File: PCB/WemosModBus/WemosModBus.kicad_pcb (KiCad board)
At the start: 2 copper layers, 38.1 x 60.3 mm, 12 parts, among them J1 Relay output, J2 Power, J3 Enable ModBus, M1 hw-726, U1 WeMos_mini, U2 MH-MINI-360

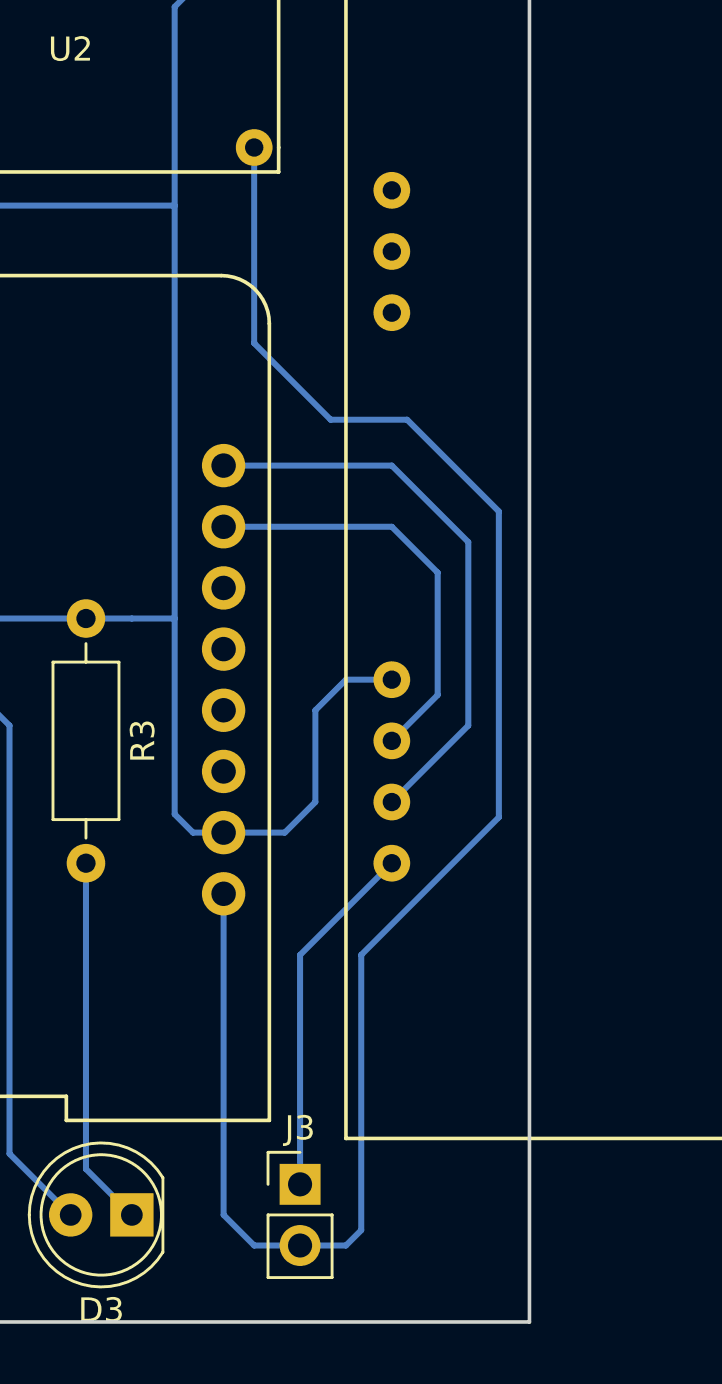
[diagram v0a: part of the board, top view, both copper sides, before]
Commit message: Made ModBus enable jumper break/connect TX instead of power to the TTL circuit.
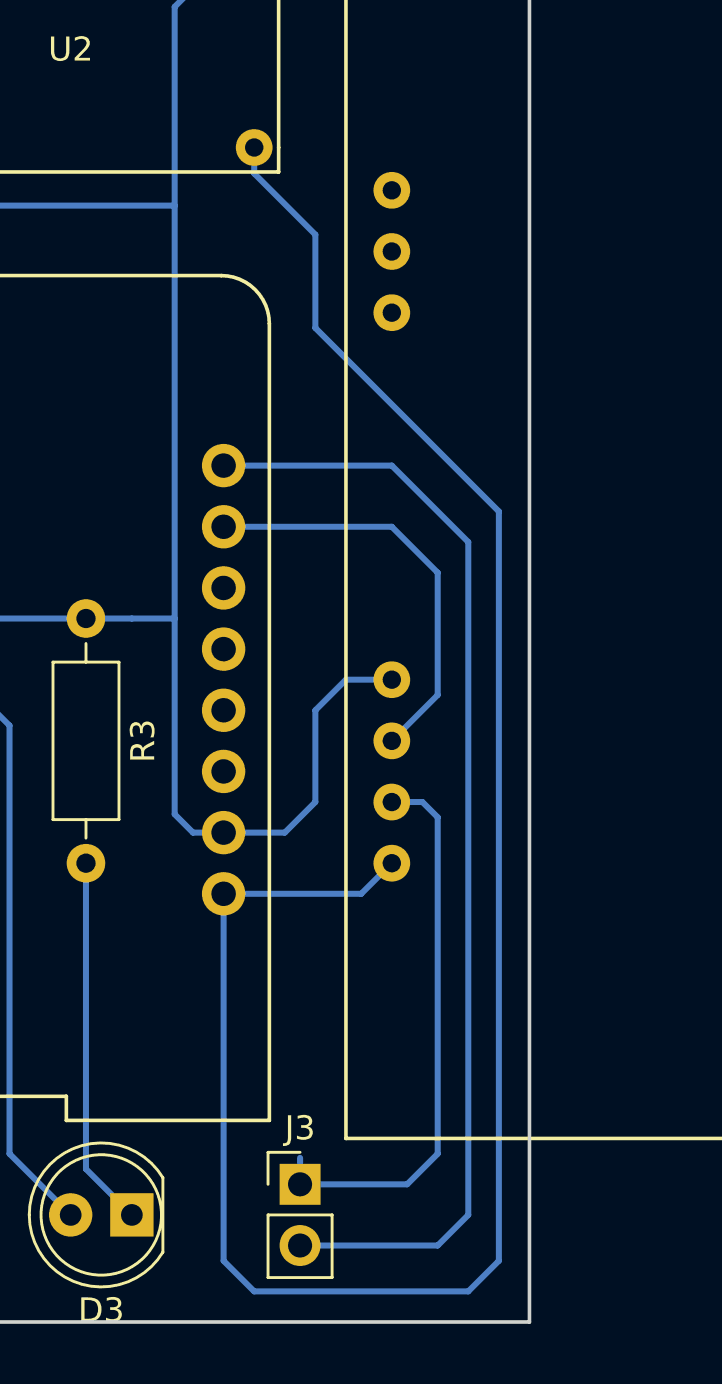
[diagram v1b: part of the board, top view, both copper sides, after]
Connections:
- M1 pad 1: Net-(J3-Pad1) -> Net-(M1-Pad1)
- M1 pad 2: Net-(M1-Pad2) -> Net-(J3-Pad1)
- U1 pad 1: Net-(J3-Pad2) -> Net-(M1-Pad1)
- U1 pad 8: Net-(M1-Pad2) -> Net-(J3-Pad2)
- U2 pad OUT+: Net-(J3-Pad2) -> Net-(M1-Pad1)
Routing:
- net Net-(M1-Pad1): track 0.00 -> 85.7 mm
- net Net-(J3-Pad2): track 73.2 -> 46.9 mm
- net Net-(M1-Pad2): track 23.6 -> 0.00 mm
- net Net-(J3-Pad1): track 14.9 -> 23.5 mm

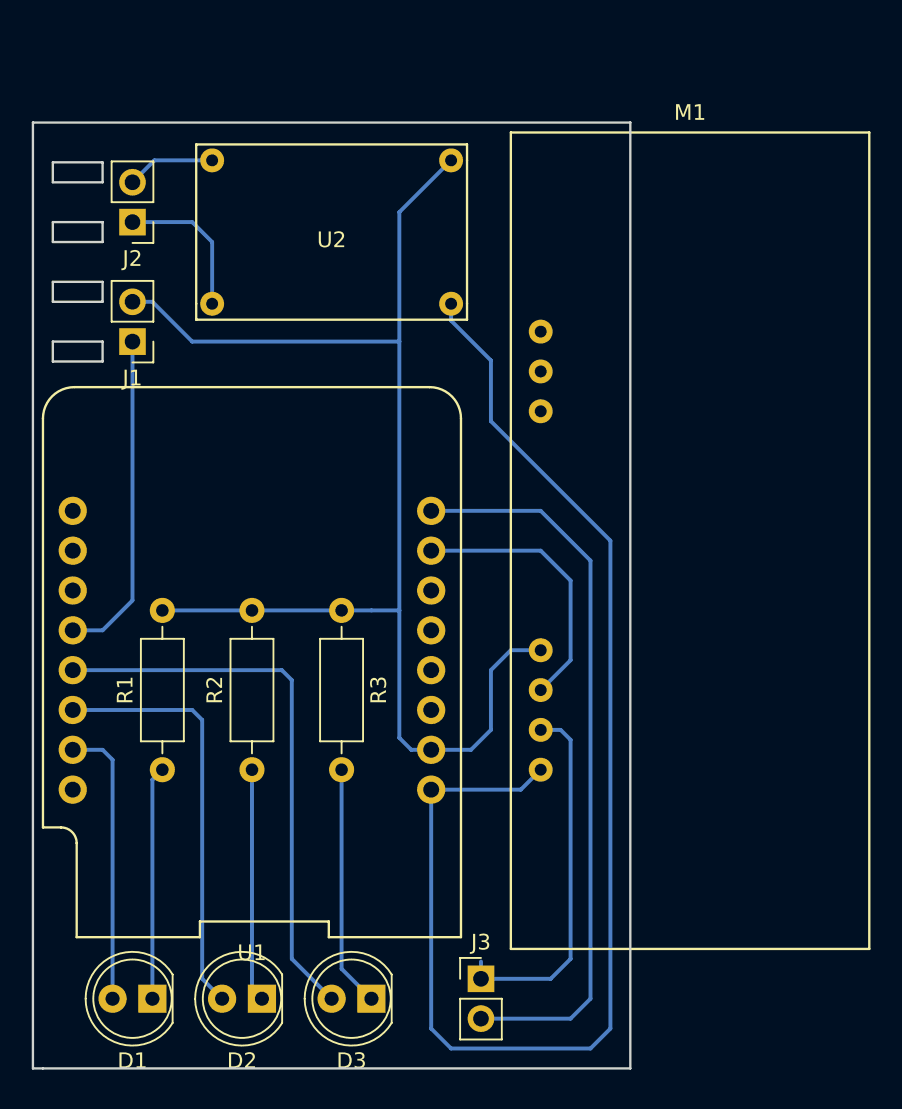
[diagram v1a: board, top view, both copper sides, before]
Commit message: Updates: connect -, gnd and earth, connect ModBus A+ and B- to pads
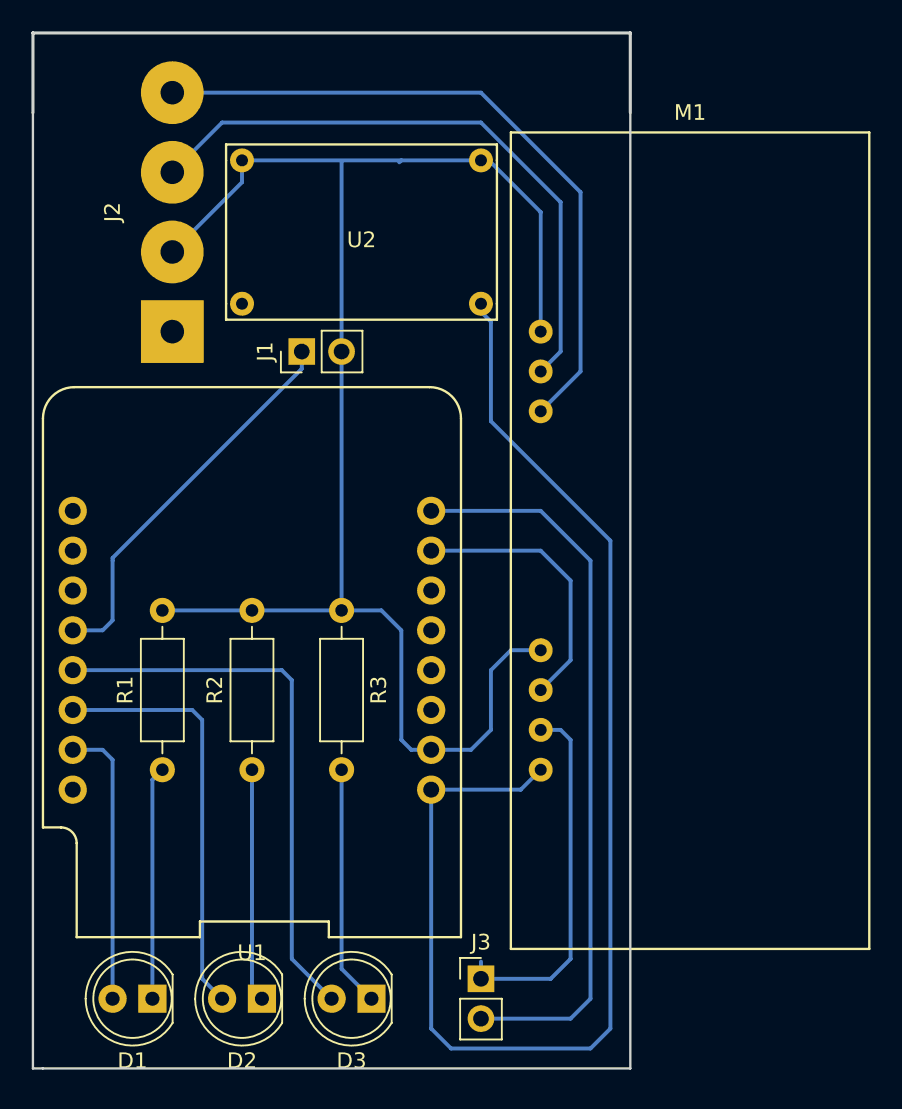
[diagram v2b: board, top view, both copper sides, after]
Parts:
- J2: footprint Connector_PinHeader_2.54mm:PinHeader_1x02_P2.54mm_Vertical -> Connector_Wire:SolderWirePad_1x04_P5.08mm_Drill1.5mm
- moved J1 10.8 mm to (108.6, 94.0), turned to 90 degrees
- moved J2 7.43 mm to (100.3, 92.7), turned to 90 degrees
- moved U2 1.91 mm to (112.4, 86.4)
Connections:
- J2 pad 2: Net-(J2-Pad2) -> Net-(J1-Pad2)
- M1 pad 5: Net-(M1-Pad5) -> Net-(J2-Pad4)
- M1 pad 6: Net-(M1-Pad6) -> Net-(J2-Pad3)
- M1 pad 7: Net-(M1-Pad7) -> Net-(J1-Pad2)
- U2 pad IN-: Net-(J2-Pad2) -> Net-(J1-Pad2)
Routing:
- net Net-(J2-Pad4): track 0.00 -> 43.7 mm
- net Net-(J2-Pad3): track 0.00 -> 39.5 mm
- net Net-(J1-Pad2): track 85.6 -> 100.7 mm
- net Net-(J2-Pad1): track 9.54 -> 0.00 mm
- net Net-(J2-Pad2): track 5.66 -> 0.00 mm
- net Net-(J1-Pad1): track 21.1 -> 24.9 mm
- net Net-(M1-Pad1): track 85.7 -> 84.9 mm
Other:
- board size 38.1 x 60.3 mm -> 38.1 x 66 mm
- board text added: "WeMos+ModBus anderskvist@gmail.com"
- board text removed: "WeMos+ModBus Anders Kvist anderskvist@gmail.com"

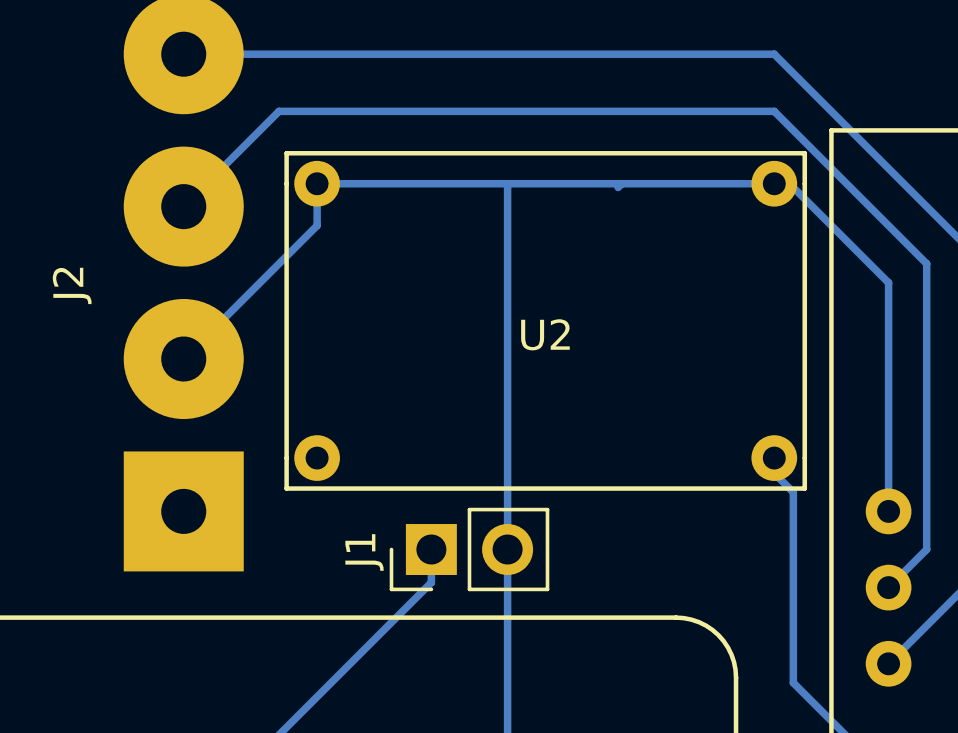
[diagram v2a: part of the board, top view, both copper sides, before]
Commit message: Added missing wire.
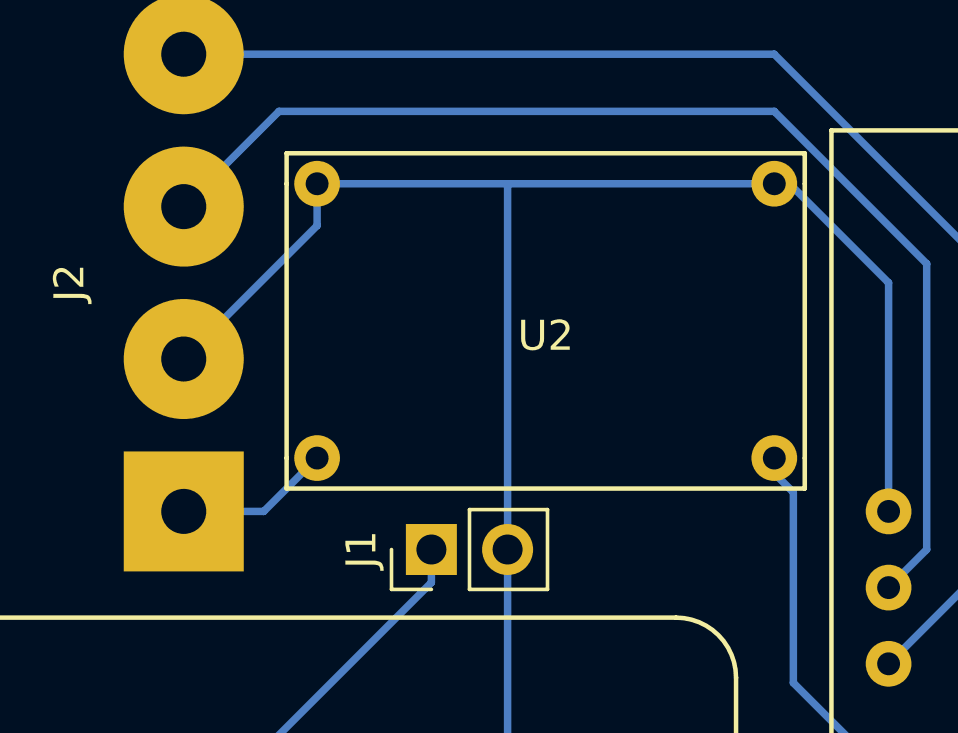
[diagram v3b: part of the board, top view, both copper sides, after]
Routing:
- net Net-(J2-Pad1): track 0.00 -> 5.18 mm
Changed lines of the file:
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@@
     (thickness 1.6)
     (drawings 8)
-    (tracks 78)
+    (tracks 80)
     (zones 0)
     (modules 12)
@@
     (0 F.Cu signal)
     (31 B.Cu signal)
-    (32 B.Adhes user)
-    (33 F.Adhes user)
-    (34 B.Paste user)
-    (35 F.Paste user)
-    (36 B.SilkS user)
-    (37 F.SilkS user)
-    (38 B.Mask user)
-    (39 F.Mask user)
-    (40 Dwgs.User user)
-    (41 Cmts.User user)
-    (42 Eco1.User user)
-    (43 Eco2.User user)
+    (32 B.Adhes user hide)
+    (33 F.Adhes user hide)
+    (34 B.Paste user hide)
+    (35 F.Paste user hide)
+    (36 B.SilkS user hide)
+    (37 F.SilkS user hide)
+    (38 B.Mask user hide)
+    (39 F.Mask user hide)
+    (40 Dwgs.User user hide)
+    (41 Cmts.User user hide)
+    (42 Eco1.User user hide)
+    (43 Eco2.User user hide)
     (44 Edge.Cuts user)
-    (45 Margin user)
-    (46 B.CrtYd user)
-    (47 F.CrtYd user)
-    (48 B.Fab user)
-    (49 F.Fab user)
+    (45 Margin user hide)
+    (46 B.CrtYd user hide)
+    (47 F.CrtYd user hide)
+    (48 B.Fab user hide)
+    (49 F.Fab user hide)
   )
   (setup
@@
   (segment (start 116.84 119.38) (end 115.57 119.38) (width 0.25) (layer B.Cu) (net 11))
   (segment (start 123.825 85.09) (end 123.825 92.71) (width 0.25) (layer B.Cu) (net 11))
-  (segment (start 114.808 81.915) (end 114.935 81.788) (width 0.25) (layer B.Cu) (net 11))
   (segment (start 120.523 81.788) (end 123.825 85.09) (width 0.25) (layer B.Cu) (net 11))
-  (segment (start 104.775 81.788) (end 120.015 81.788) (width 0.25) (layer B.Cu) (net 11))
   (segment (start 111.125 93.98) (end 111.125 110.49) (width 0.25) (layer B.Cu) (net 11))
   (segment (start 114.935 111.76) (end 114.935 118.745) (width 0.25) (layer B.Cu) (net 11))
@@
   (segment (start 104.775 83.185) (end 104.775 81.788) (width 0.25) (layer B.Cu) (net 11))
   (segment (start 100.33 87.63) (end 104.775 83.185) (width 0.25) (layer B.Cu) (net 11))
-  (segment (start 111.125 93.98) (end 111.125 81.915) (width 0.25) (layer B.Cu) (net 11))
+  (segment (start 111.125 93.98) (end 111.125 81.788) (width 0.25) (layer B.Cu) (net 11))
+  (segment (start 104.775 81.788) (end 111.125 81.788) (width 0.25) (layer B.Cu) (net 11))
+  (segment (start 111.125 81.788) (end 120.015 81.788) (width 0.25) (layer B.Cu) (net 11))
+  (segment (start 102.997 92.71) (end 104.775 90.932) (width 0.25) (layer B.Cu) (net 12))
+  (segment (start 100.33 92.71) (end 102.997 92.71) (width 0.25) (layer B.Cu) (net 12))
   (segment (start 96.52 120.015) (end 96.52 135.89) (width 0.25) (layer B.Cu) (net 13))
   (segment (start 95.885 119.38) (end 96.52 120.015) (width 0.25) (layer B.Cu) (net 13))

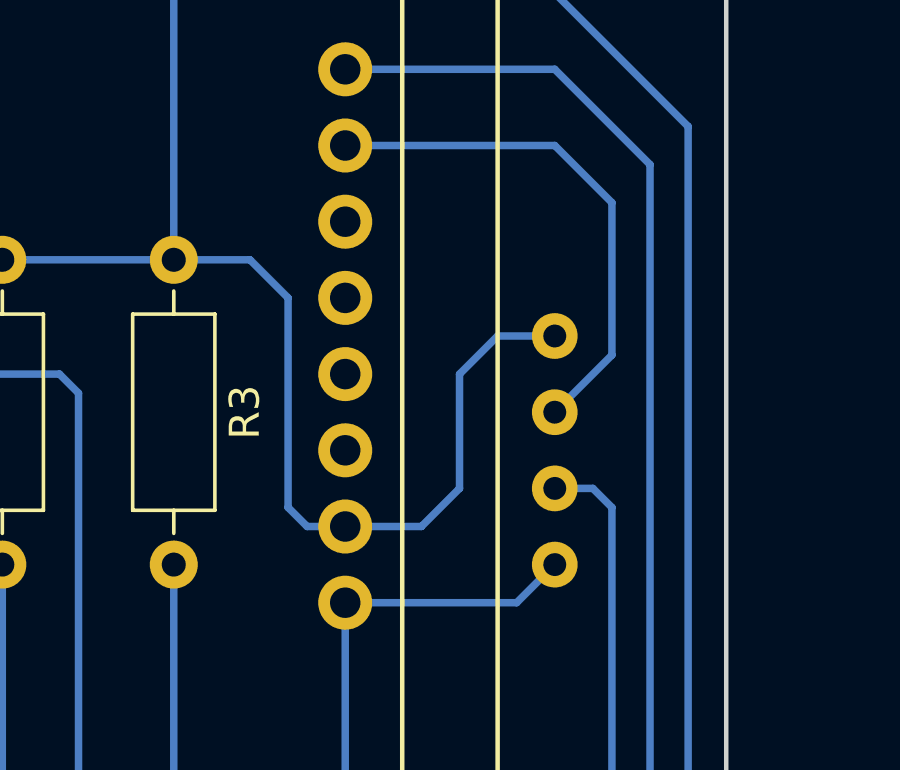
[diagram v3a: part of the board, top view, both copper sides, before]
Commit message: Adding pads for jumper wires if software serial is going to be tested.
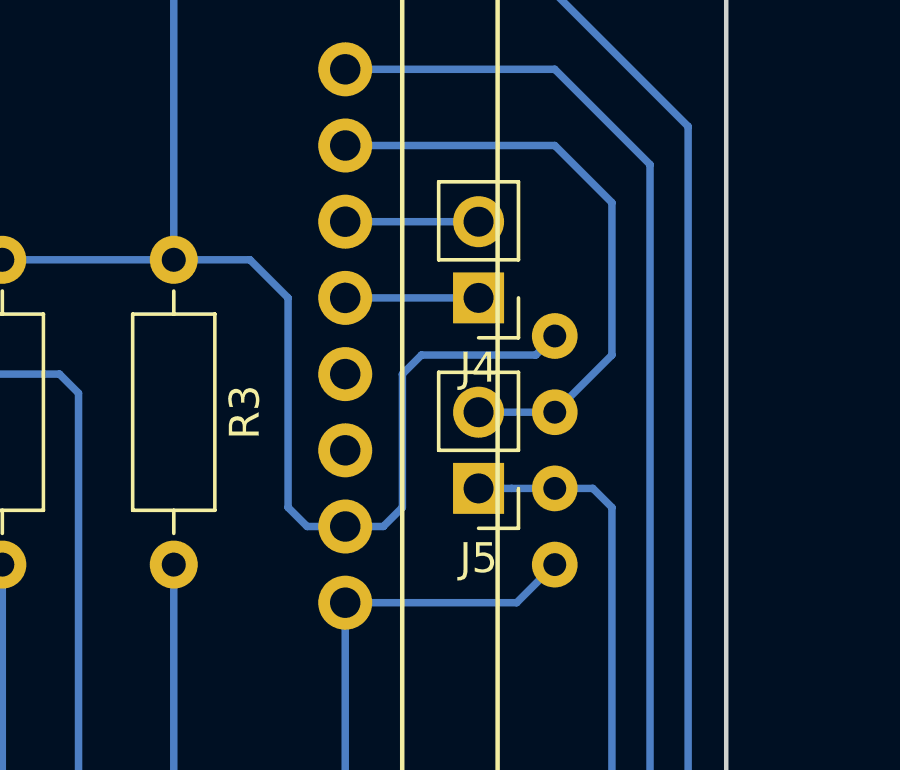
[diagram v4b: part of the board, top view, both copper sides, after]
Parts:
- added J4: Software Seriel test #1, Connector_PinHeader_2.54mm:PinHeader_1x02_P2.54mm_Vertical, F.Cu at (121.3, 111.8)
- added J5: Software Seriel test #2, Connector_PinHeader_2.54mm:PinHeader_1x02_P2.54mm_Vertical, F.Cu at (121.3, 118.1)
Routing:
- net Net-(J4-Pad2): track 0.00 -> 4.44 mm
- net Net-(J4-Pad1): track 0.00 -> 4.44 mm
- net Net-(J5-Pad2): track 17.5 -> 20.0 mm
- net Net-(J3-Pad1): track 23.5 -> 26.0 mm
